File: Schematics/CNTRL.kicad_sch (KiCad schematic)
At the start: 40 parts, among them SW1 RotaryEncoder_Switch, SW2 RotaryEncoder_Switch, SW3 RotaryEncoder_Switch, SW4 RotaryEncoder_Switch

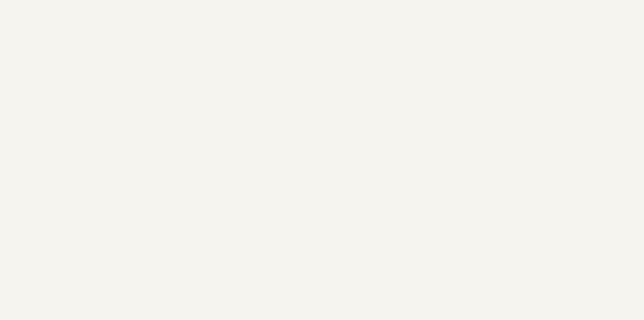
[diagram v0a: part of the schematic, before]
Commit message: Input Buffer & EEPROM
line and instrument level buffers for the input added. EEPROM added and credits attributed !
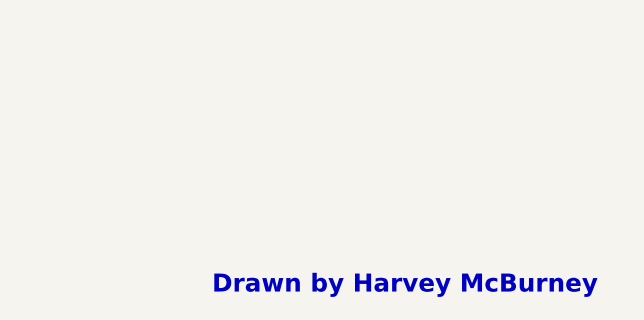
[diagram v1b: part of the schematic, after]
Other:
- note added: "Drawn by Harvey McBurney"
- title: (none) -> ENCODER CLUSTER
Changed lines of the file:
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@@
 	(generator_version "8.0")
 	(paper "A4")
+	(title_block
+		(title "ENCODER CLUSTER")
+		(date "2025-02-12")
+	)
 	(junction
 		(at 55.88 101.6)
@@
 		)
 	)
+	(text "Drawn by Harvey McBurney"
+		(exclude_from_sim no)
+		(at 199.39 169.418 0)
+		(effects
+			(font
+				(size 2 2)
+				(thickness 0.6)
+				(bold yes)
+			)
+		)
+	)
 	(global_label "ENC1_B"
 		(shape input)
@@
 		)
 		(instances
-			(project ""
+			(project "Harmoniser HAT"
 				(path "/41751dd2-97f9-4cc6-b9e6-b561e5949053/5d678f4e-03b5-43f5-b100-a64e850a5e5c"
 					(reference "#PWR018")
@@
 		)
 		(instances
-			(project ""
+			(project "Harmoniser HAT"
 				(path "/41751dd2-97f9-4cc6-b9e6-b561e5949053/5d678f4e-03b5-43f5-b100-a64e850a5e5c"
 					(reference "R1")
@@
 		)
 		(instances
-			(project ""
+			(project "Harmoniser HAT"
 				(path "/41751dd2-97f9-4cc6-b9e6-b561e5949053/5d678f4e-03b5-43f5-b100-a64e850a5e5c"
 					(reference "#PWR016")
@@
 		)
 		(instances
-			(project ""
+			(project "Harmoniser HAT"
 				(path "/41751dd2-97f9-4cc6-b9e6-b561e5949053/5d678f4e-03b5-43f5-b100-a64e850a5e5c"
 					(reference "#PWR017")
@@
 		)
 		(instances
-			(project ""
+			(project "Harmoniser HAT"
 				(path "/41751dd2-97f9-4cc6-b9e6-b561e5949053/5d678f4e-03b5-43f5-b100-a64e850a5e5c"
 					(reference "SW1")
@@
 		)
 		(instances
-			(project ""
+			(project "Harmoniser HAT"
 				(path "/41751dd2-97f9-4cc6-b9e6-b561e5949053/5d678f4e-03b5-43f5-b100-a64e850a5e5c"
 					(reference "#PWR011")
@@
 		)
 		(instances
-			(project ""
+			(project "Harmoniser HAT"
 				(path "/41751dd2-97f9-4cc6-b9e6-b561e5949053/5d678f4e-03b5-43f5-b100-a64e850a5e5c"
 					(reference "C9")

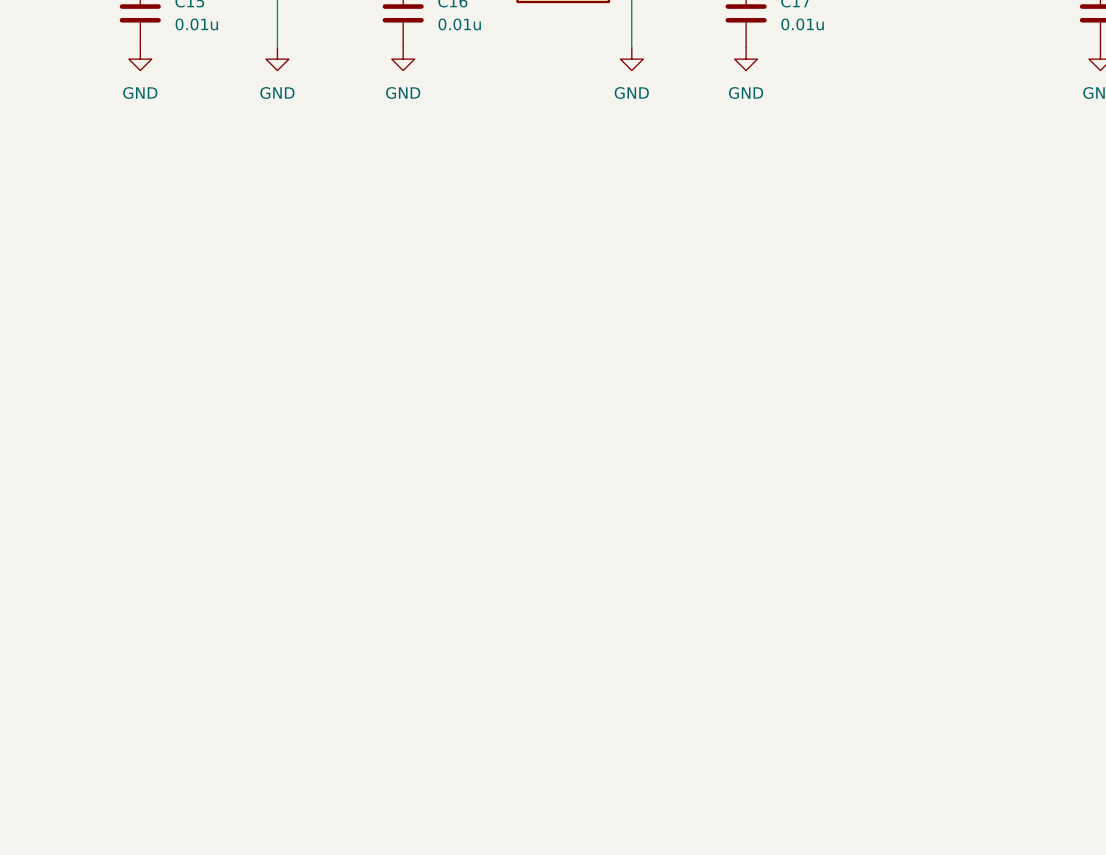
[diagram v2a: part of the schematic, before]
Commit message: Added I/O Expander
I/O Expander added, 4 spare pins, still need to decouple.
Fixed some references to 3.3V, now all 3V3.
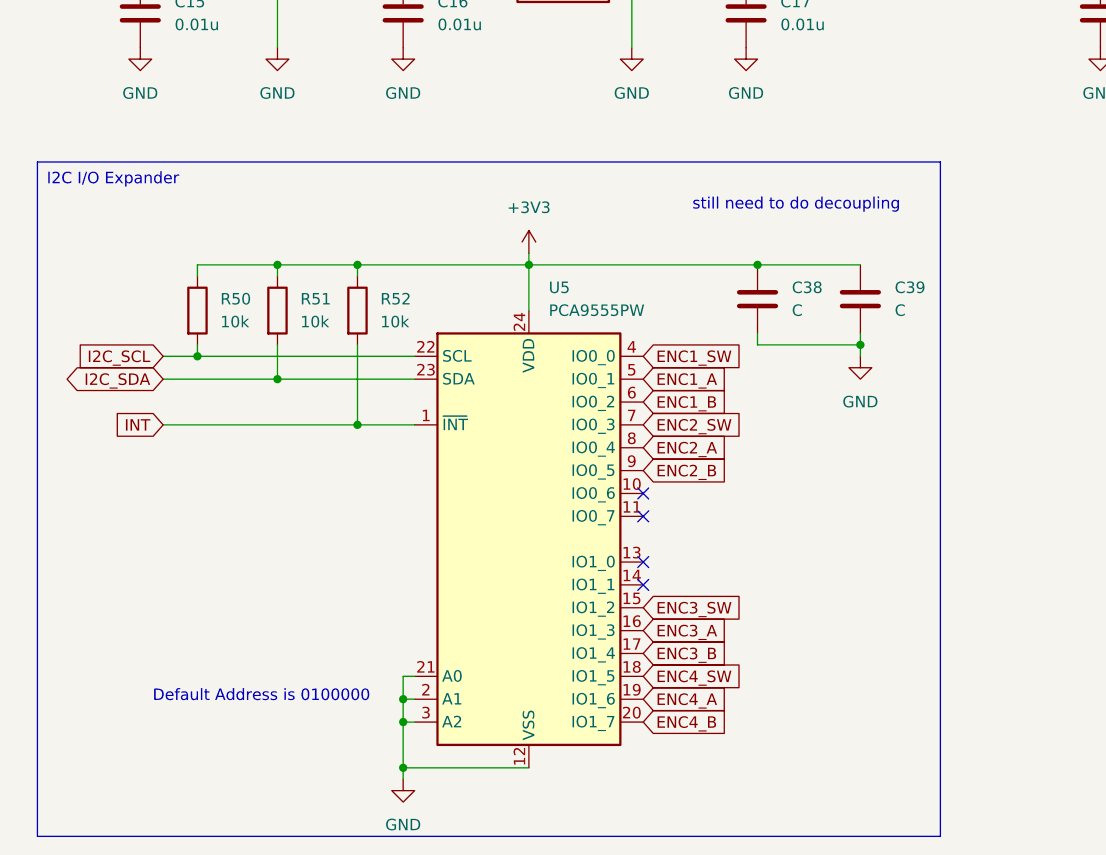
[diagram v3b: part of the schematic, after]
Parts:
- added C38, C39: C, symbol Device:C
- added R50, R51, R52: 10k, symbol Device:R
- added U5: PCA9555PW, Package_SO:TSSOP-24_4.4x7.8mm_P0.65mm, symbol Interface_Expansion:PCA9555PW
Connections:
- net +3V3: now also C38.1, C39.1, R50.1, R51.1, R52.1, U5.24 (VDD)
- net ENC1_A: now also U5.5 (IO0_1)
- net ENC1_B: now also U5.6 (IO0_2)
- net ENC1_SW: now also U5.4 (IO0_0)
- net ENC2_A: now also U5.8 (IO0_4)
- net ENC2_B: now also U5.9 (IO0_5)
- net ENC2_SW: now also U5.7 (IO0_3)
- net ENC3_A: now also U5.16 (IO1_3)
- net ENC3_B: now also U5.17 (IO1_4)
- net ENC3_SW: now also U5.15 (IO1_2)
- net ENC4_A: now also U5.19 (IO1_6)
- net ENC4_B: now also U5.20 (IO1_7)
- net ENC4_SW: now also U5.18 (IO1_5)
- net GND: now also C38.2, C39.2, U5.12 (VSS), U5.2 (A1), U5.21 (A0), U5.3 (A2)
- new net I2C_SCL: R50.2, U5.22 (SCL)
- new net I2C_SDA: R51.2, U5.23 (SDA)
- new net INT: R52.2, U5.1 (~{INT})
- no-connect marks 0 -> 4
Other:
- note added: "Default Address is 0100000"
- note added: "still need to do decoupling"
- title: ENCODER CLUSTER -> Control

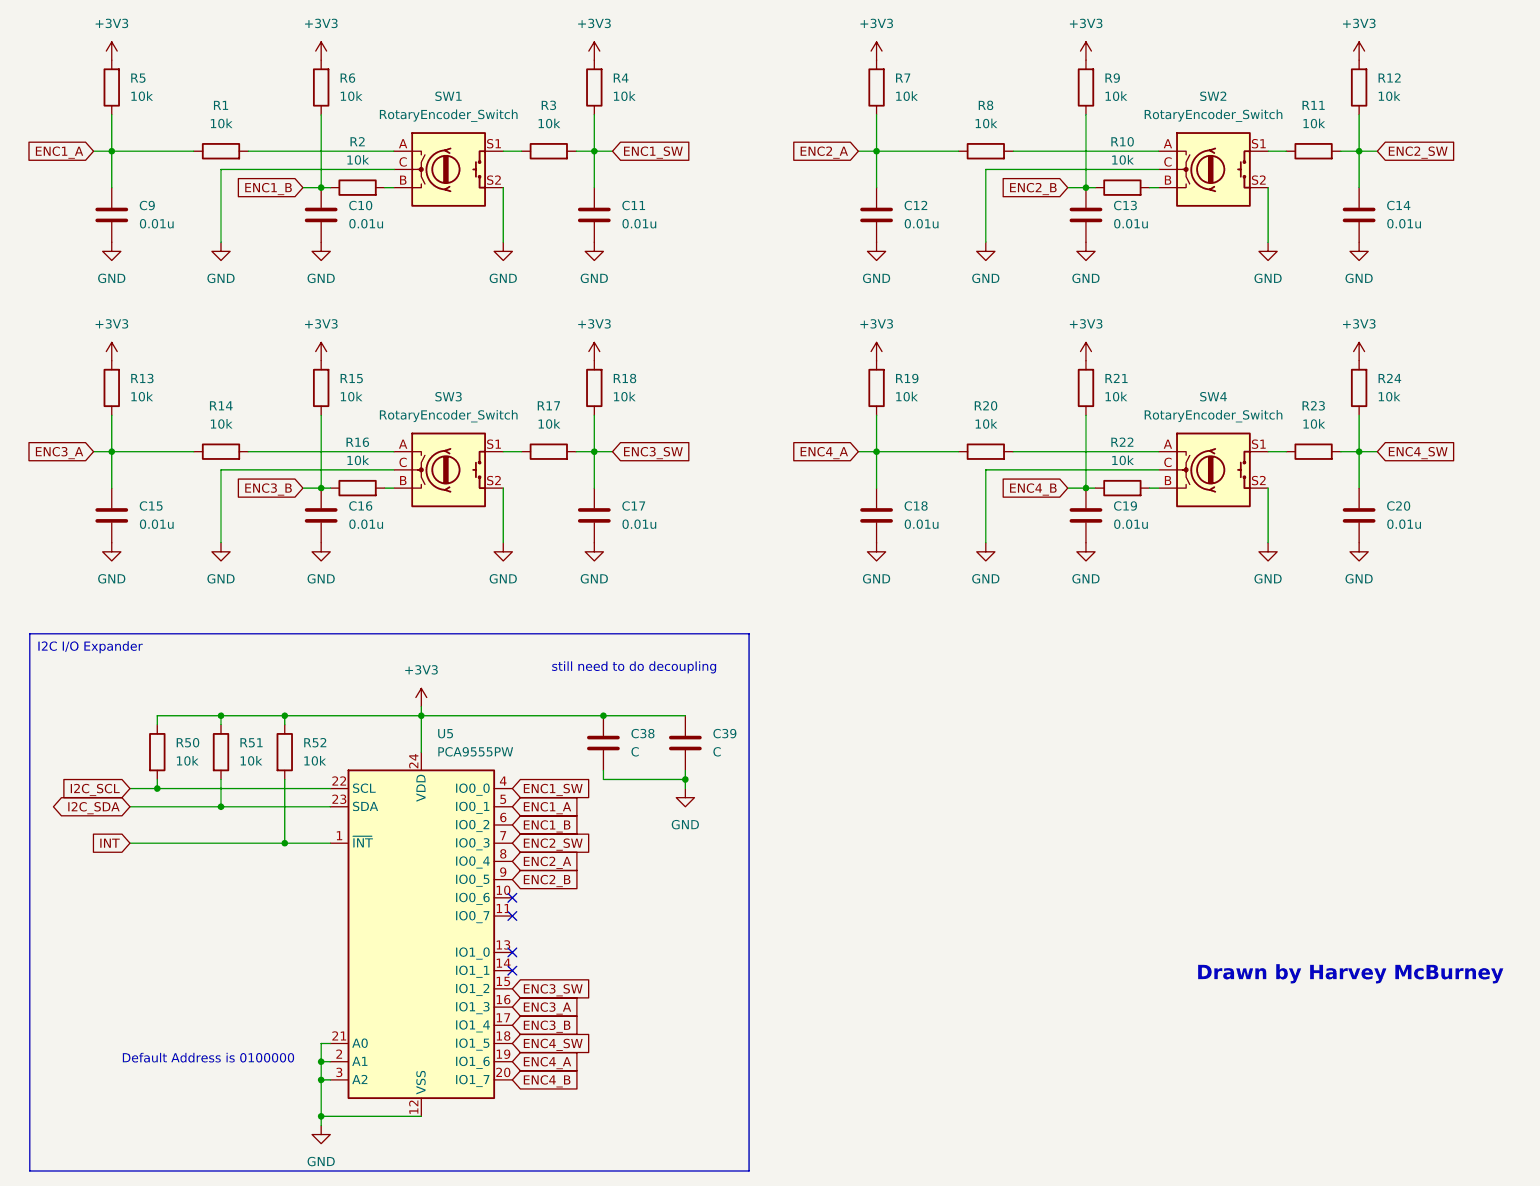
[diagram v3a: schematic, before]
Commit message: Started adding footprints, changed values.
Added footprints for most components. need to check in uni which sizes are available and what will need to be ordered from mouser.
Changed line in/out to TRS as this will be more reliable and added 0 ohm resistor options to bypass mono input and use line in/out as stereo.
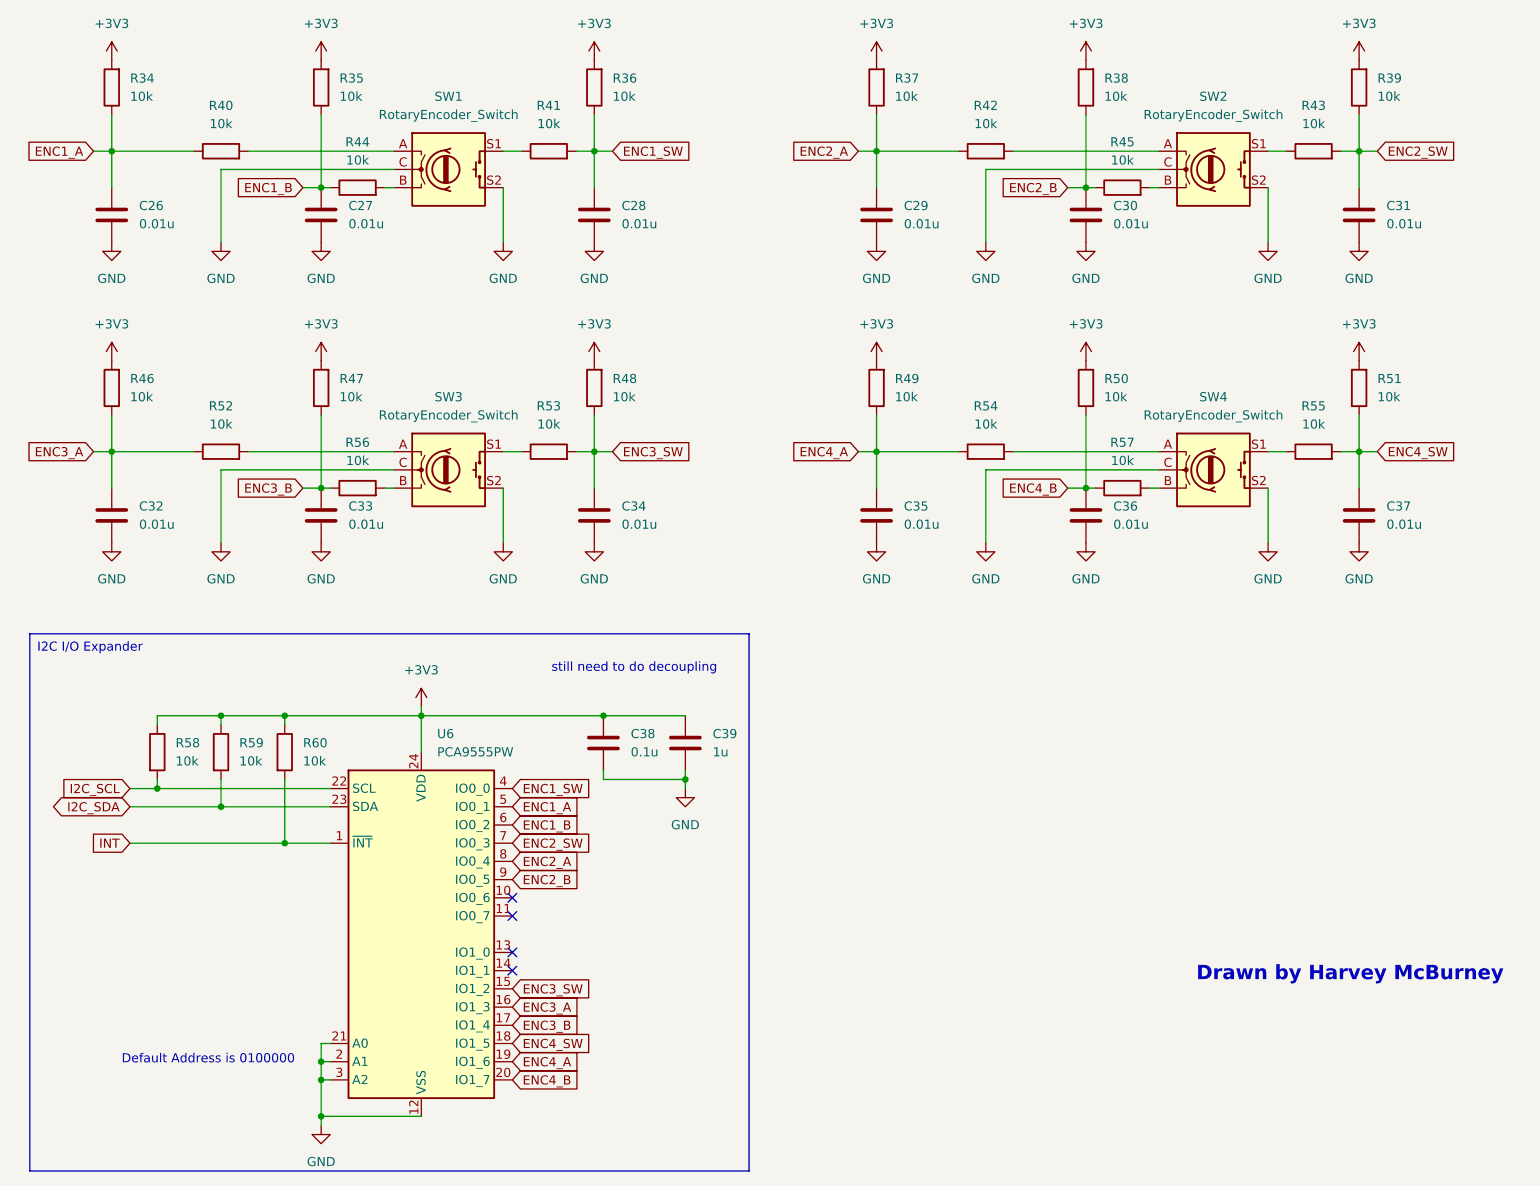
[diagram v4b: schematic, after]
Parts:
- C38: value C -> 0.1u
- C39: value C -> 1u
- R34: renamed from R5; footprint (none) -> Resistor_SMD:R_0603_1608Metric_Pad0.98x0.95mm_HandSolder
- R35: renamed from R6; footprint (none) -> Resistor_SMD:R_0603_1608Metric_Pad0.98x0.95mm_HandSolder
- R36: renamed from R4; footprint (none) -> Resistor_SMD:R_0603_1608Metric_Pad0.98x0.95mm_HandSolder
- R37: renamed from R7; footprint (none) -> Resistor_SMD:R_0603_1608Metric_Pad0.98x0.95mm_HandSolder
- R38: renamed from R9; footprint (none) -> Resistor_SMD:R_0603_1608Metric_Pad0.98x0.95mm_HandSolder
- R39: renamed from R12; footprint (none) -> Resistor_SMD:R_0603_1608Metric_Pad0.98x0.95mm_HandSolder
- R40: renamed from R1; footprint (none) -> Resistor_SMD:R_0603_1608Metric_Pad0.98x0.95mm_HandSolder
- R41: renamed from R3; footprint (none) -> Resistor_SMD:R_0603_1608Metric_Pad0.98x0.95mm_HandSolder
- R42: renamed from R8; footprint (none) -> Resistor_SMD:R_0603_1608Metric_Pad0.98x0.95mm_HandSolder
- R43: renamed from R11; footprint (none) -> Resistor_SMD:R_0603_1608Metric_Pad0.98x0.95mm_HandSolder
- R44: renamed from R2; footprint (none) -> Resistor_SMD:R_0603_1608Metric_Pad0.98x0.95mm_HandSolder
- R45: renamed from R10; footprint (none) -> Resistor_SMD:R_0603_1608Metric_Pad0.98x0.95mm_HandSolder
- R46: renamed from R13; footprint (none) -> Resistor_SMD:R_0603_1608Metric_Pad0.98x0.95mm_HandSolder
- R47: renamed from R15; footprint (none) -> Resistor_SMD:R_0603_1608Metric_Pad0.98x0.95mm_HandSolder
- R48: renamed from R18; footprint (none) -> Resistor_SMD:R_0603_1608Metric_Pad0.98x0.95mm_HandSolder
- R49: renamed from R19; footprint (none) -> Resistor_SMD:R_0603_1608Metric_Pad0.98x0.95mm_HandSolder
- R50: renamed from R21; footprint (none) -> Resistor_SMD:R_0603_1608Metric_Pad0.98x0.95mm_HandSolder
- R51: renamed from R24; footprint (none) -> Resistor_SMD:R_0603_1608Metric_Pad0.98x0.95mm_HandSolder
- R52: renamed from R14; footprint (none) -> Resistor_SMD:R_0603_1608Metric_Pad0.98x0.95mm_HandSolder
- R53: renamed from R17; footprint (none) -> Resistor_SMD:R_0603_1608Metric_Pad0.98x0.95mm_HandSolder
- R54: renamed from R20; footprint (none) -> Resistor_SMD:R_0603_1608Metric_Pad0.98x0.95mm_HandSolder
- R55: renamed from R23; footprint (none) -> Resistor_SMD:R_0603_1608Metric_Pad0.98x0.95mm_HandSolder
- R56: renamed from R16; footprint (none) -> Resistor_SMD:R_0603_1608Metric_Pad0.98x0.95mm_HandSolder
- R57: renamed from R22; footprint (none) -> Resistor_SMD:R_0603_1608Metric_Pad0.98x0.95mm_HandSolder
- R58: renamed from R50; footprint (none) -> Resistor_SMD:R_0603_1608Metric_Pad0.98x0.95mm_HandSolder
- R59: renamed from R51; footprint (none) -> Resistor_SMD:R_0603_1608Metric_Pad0.98x0.95mm_HandSolder
- R60: renamed from R52; footprint (none) -> Resistor_SMD:R_0603_1608Metric_Pad0.98x0.95mm_HandSolder
- SW1, SW2, SW3, SW4: footprint (none) -> Rotary_Encoder:RotaryEncoder_Bourns_Vertical_PEC12R-3x17F-Sxxxx
- renumbered C9 to C26, C10 to C27, C11 to C28, C12 to C29, C13 to C30, C14 to C31, C15 to C32, C16 to C33, C17 to C34, C18 to C35, C19 to C36, C20 to C37, U5 to U6
